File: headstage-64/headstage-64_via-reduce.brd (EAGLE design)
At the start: 19.3 x 19 mm, 169 parts, among them J3 GND_LINK_0201, U1 TS4231, U11 10M08DC, U12 LT3463, U13 DAC5311, U14 TS4231, U15 INA826, U16 TLV70733, U17 TLV70712, U18 TLV70733, U19 DS90UB913A_WQFN, U2 MPU9250_QFN_NO-PAD, U22 TPS62621, U25 TPL0501_UQFN, U3 CAT4016_QFN, U4 OPA170, U5 TS4231, U6 TS4231, U7 RHD2064_BGA, U8 ADG1401, U9 TLV70725

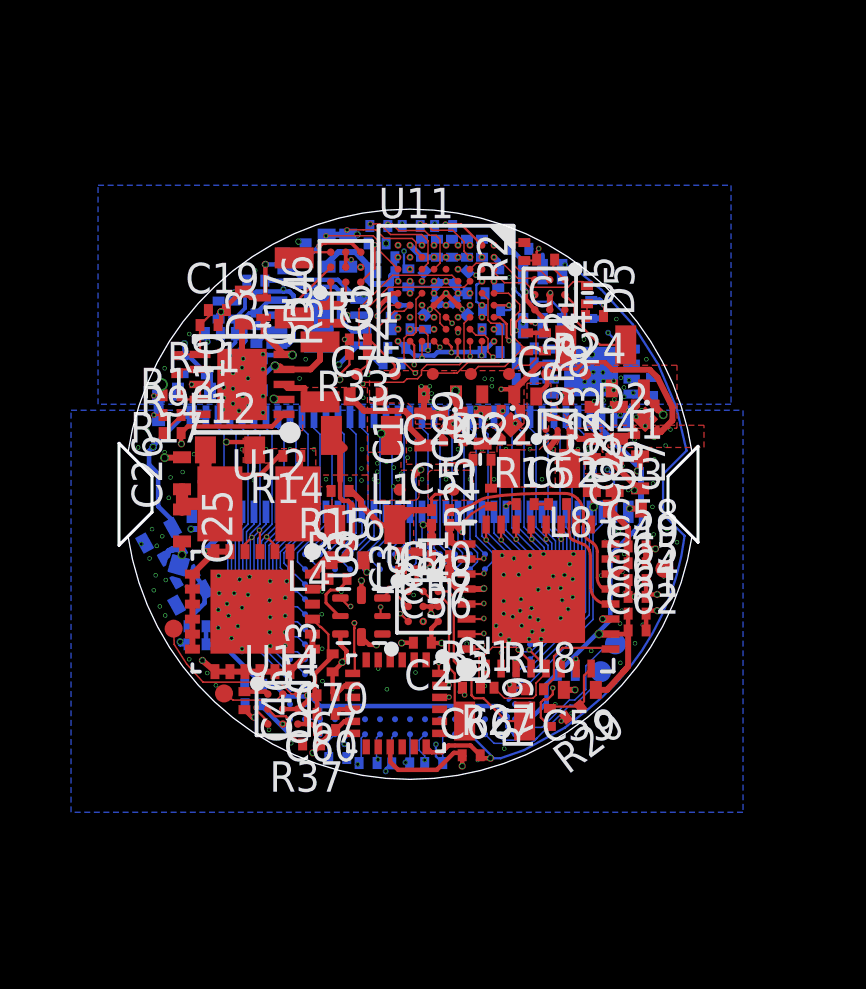
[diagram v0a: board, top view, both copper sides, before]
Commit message: Headstage-64 updates following testing
- Added 50 MHz crystal oscillator to drive FPGA PLL
- LED driver now gets serial data via common MOSI line instead of
dedicated SDO. Clock line is still separate since it acts like the LED
driver's clock and CS together.
- LED driver's blank pin is now tied to CRC_ERROR/C5 on FPGA
- Removed one status LED and instead routed serializer GPIO0 to FPGA
- Increased size of programming pads
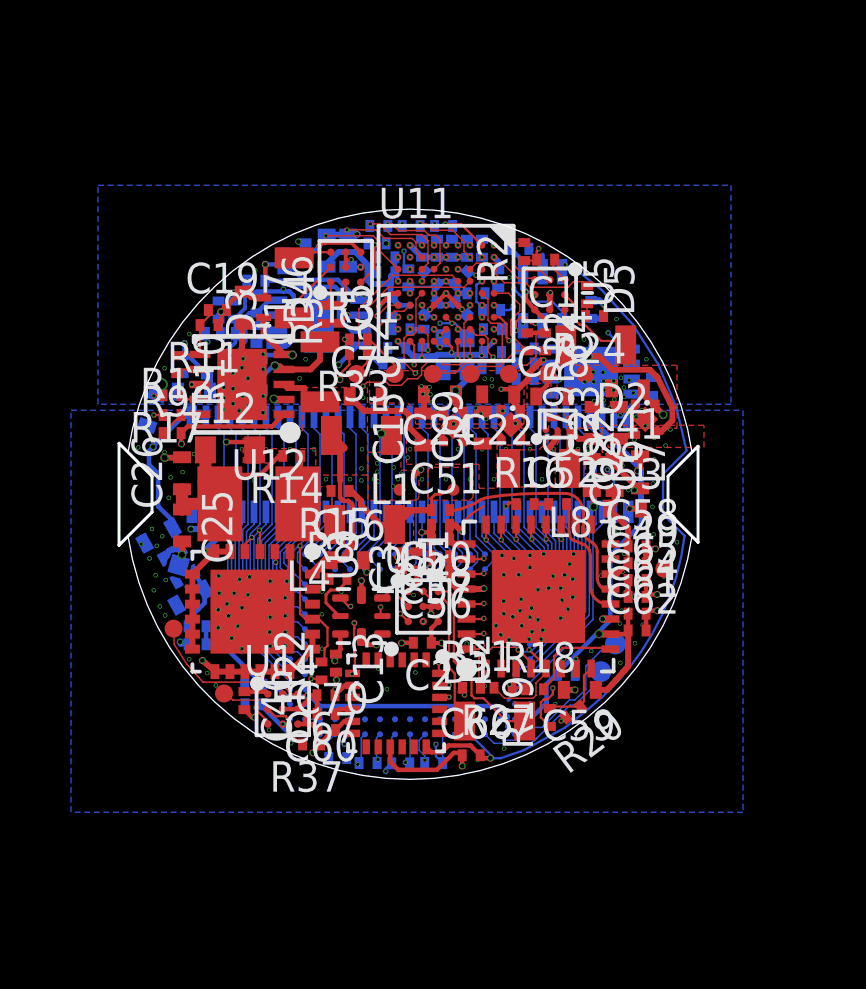
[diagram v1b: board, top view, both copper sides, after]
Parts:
- removed D6: XZVGR155W, jonnew:LED-0201T
- removed J3: GND_LINK_0201, jonnew:0201_LINK
- removed R25: 2k, jonnew:0201T
- added C54: 10nF, jonnew:0201T
- added L13: BLM15PX601SN1D, jonnew:0402T
- added R22: 10k, jonnew:0201T
- added U26: ASCO-50.000MHZ-EK-T3, jonnew:ASCO
- TP1, TP12, TP2, TP3, TP4, TP5, TP6: device jonnew:B0.4MM -> jonnew:TP06R
- moved C13 0.11 mm to (-2.47, -5.63), turned to 270 degrees
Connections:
- net STATUS_B renamed STATUS
- removed net GPO0: TP7.TP, U19.15
- removed net LED_SIN: U11.F1, U3.2
- removed net N$39: D6.2, R25.2
- removed net SDO: U11.E3, U13.3, U2.9
- removed net STATUS_A: D6.1, U11.C2
- new net GPIO0: TP7.TP, U11.C2, U19.15
- new net LED_BLANK: R22.2, U11.C5, U3.21
- new net MOSI: U11.E3, U13.3, U2.9, U3.2
- new net N$37: U11.F1, U26.3
- net +3V3: now also C54.1, R22.1, U26.1, U26.4; no longer R25.1
- net AGND: now also L13.2; no longer J3.1
- net GND: now also C54.2, L13.1, U26.2; no longer J3.2, U3.21
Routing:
- net MOSI: track 0.00 -> 28.1 mm, vias 0 -> 6
- net LED_BLANK: track 0.00 -> 24.4 mm, vias 0 -> 2
- net SDO: track 22.0 -> 0.00 mm, vias 4 -> 0
- net GPIO0: track 0.00 -> 21.5 mm, vias 0 -> 3
- net LED_SIN: track 19.5 -> 0.00 mm, vias 2 -> 0
- net STATUS_A: track 8.32 -> 0.00 mm, vias 2 -> 0
- net GND: track 41.7 -> 38.3 mm, vias 184 -> 186
- net N$37: track 0.00 -> 3.38 mm, vias 0 -> 2
- net GPO0: track 1.99 -> 0.00 mm, vias 2 -> 0
- net +3V3: track 30.4 -> 31.5 mm, vias 21 -> 23
- net N$39: track 0.95 -> 0.00 mm
- net +2V5: track 23.1 -> 23.4 mm, vias 6 -> 8
- added copper zone on layer 4, net +2V5
- added copper zone on layer 1, net GPIO0
- added copper zone on layer 2, net GPIO0
- added copper zone on layer 3, net GPIO0
- added copper zone on layer 1, net LED_BLANK
- added copper zone on layer 3, net LED_BLANK
- added copper zone on layer 1, net MOSI
- added copper zone on layer 16, net MOSI
- added copper zone on layer 2, net MOSI
- added copper zone on layer 3, net MOSI
- added copper zone on layer 16, net N$37
- added copper zone on layer 2, net N$37
- removed copper zone on layer 1, net GPO0
- removed copper zone on layer 3, net GPO0
- removed copper zone on layer 1, net LED_SIN
- removed copper zone on layer 3, net LED_SIN
- removed copper zone on layer 1, net SDO
- removed copper zone on layer 16, net SDO
- removed copper zone on layer 2, net SDO
- removed copper zone on layer 3, net SDO
- removed copper zone on layer 1, net STATUS_A
- removed copper zone on layer 3, net STATUS_A

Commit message: Updates due to production questions from speedy
- Space added between some components
- 3.3V stub removed from headstage-64
- Intan AUXOUTs routed to test points on both boards
- Crystal's re-routed to drive FPGA clock pins that interface with an
avaialble PLL. Previous routing went to clock pins that had no PLL on
both designs.
- Some pins swapping to simplfy routing on both boards.
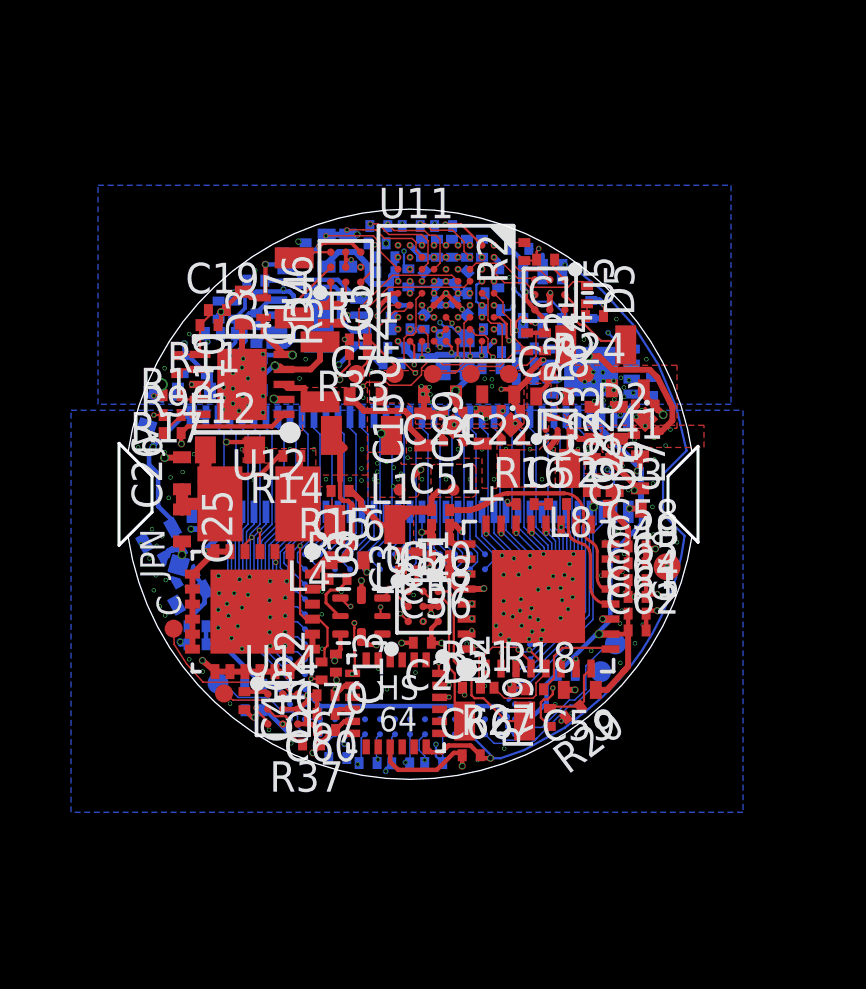
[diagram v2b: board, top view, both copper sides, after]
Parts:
- added TP13: VCC, jonnew:TP07R
- TP7: device jonnew:TP06R -> jonnew:TP09R
- moved C30 0.20 mm to (-5.20, -7.20)
- moved TP7 0.11 mm to (8.57, -2.42)
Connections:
- new net N$39: TP13.TP, U7.N16
- net DAC_CS: now also U11.C2; no longer U11.C4
- net DATA4: now also U11.B6; no longer U11.G3
- net ENV2: now also U11.F1; no longer U11.D8
- net ENV4: now also U11.G3; no longer U11.B6
- net GPIO0: now also U11.A5; no longer U11.C2
- net N$37: now also U11.D8; no longer U11.F1
- net STIM_NULL: now also U11.C4; no longer U11.A5
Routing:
- net N$39: track 0.00 -> 4.06 mm
- net ENV4: track 23.2 -> 20.2 mm, vias 2 -> 3
- net ENV2: track 4.43 -> 1.50 mm
- net GPIO0: track 21.5 -> 18.8 mm
- net DATA4: track 20.2 -> 22.1 mm, vias 3 -> 2
- net +3V3: track 31.5 -> 30.2 mm
- net DAC_CS: track 4.53 -> 3.73 mm
- net DIN0: track 9.56 -> 8.76 mm
- net STIM_NULL: track 8.02 -> 7.27 mm
- net DIN7: track 11.1 -> 10.4 mm
- net DIN6: track 10.0 -> 9.43 mm
- net DIN10: track 13.6 -> 13.1 mm
- net DIN8: track 11.7 -> 11.1 mm
- net TDI: track 5.15 -> 4.62 mm
- net GND: vias 186 -> 187
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- added copper zone on layer 1, net ENV4
- added copper zone on layer 3, net ENV4
- removed copper zone on layer 3, net DATA4
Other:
- board text added: "+"
- board text added: "-"
- board text added: "0"
- board text added: "C"
- board text added: "COHLv1.2"
- board text added: "G"
- board text added: "HS 64"
- board text added: "HS-64 Rev 1.1"
- board text added: "JPN"
- board text added: "JPN&JV MIT,'18"
- board text added: "JV"
- board text removed: "HS-64 Rev 1.0"
- board text removed: "JPN,JV COHL v1.2"

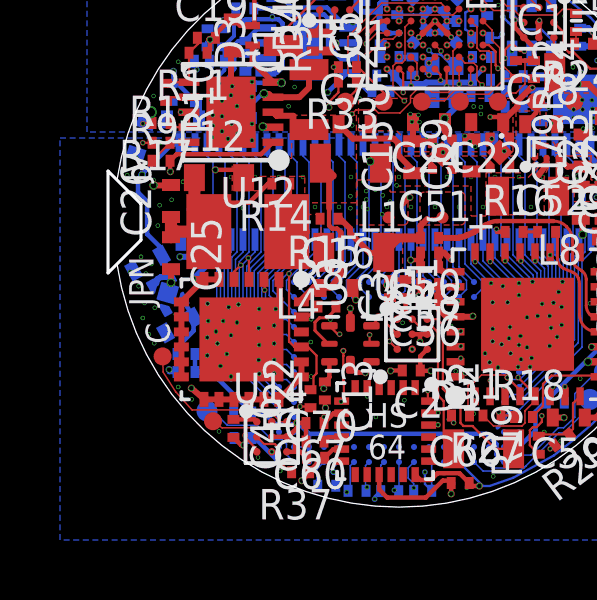
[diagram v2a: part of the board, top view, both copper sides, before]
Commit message: Added AGND testpoints to bottom of headstage-64 and headstage-256
- So that people can actually use the other IO test points...
- These are ready for production
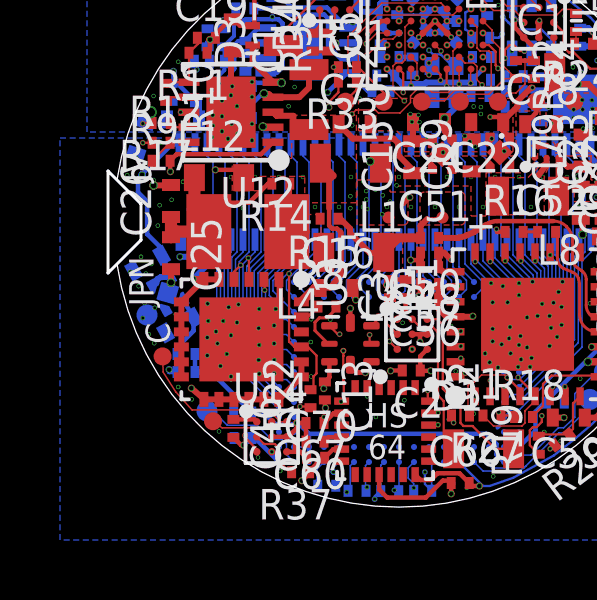
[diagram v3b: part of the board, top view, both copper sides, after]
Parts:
- added TP14: VCC, jonnew:TP07R
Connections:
- net AGND: now also TP14.TP
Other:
- board text added: "IN2"
- board text added: "IN3"
- board text added: "O"
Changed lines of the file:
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@@
 <setting verticaltext="up"/>
 </settings>
-<grid distance="0.05" unitdist="mm" unit="mm" style="lines" multiple="1" display="yes" altdistance="0.1" altunitdist="mm" altunit="mm"/>
+<grid distance="0.1" unitdist="mm" unit="mm" style="lines" multiple="1" display="yes" altdistance="0.1" altunitdist="mm" altunit="mm"/>
 <layers>
 <layer number="1" name="Top" color="4" fill="1" visible="yes" active="yes"/>
@@
 <layer number="19" name="Unrouted" color="14" fill="1" visible="yes" active="yes"/>
 <layer number="20" name="Dimension" color="15" fill="1" visible="yes" active="yes"/>
-<layer number="21" name="tPlace" color="7" fill="1" visible="yes" active="yes"/>
+<layer number="21" name="tPlace" color="7" fill="1" visible="no" active="yes"/>
 <layer number="22" name="bPlace" color="7" fill="1" visible="yes" active="yes"/>
-<layer number="23" name="tOrigins" color="15" fill="1" visible="yes" active="yes"/>
+<layer number="23" name="tOrigins" color="15" fill="1" visible="no" active="yes"/>
 <layer number="24" name="bOrigins" color="15" fill="1" visible="yes" active="yes"/>
 <layer number="25" name="tNames" color="7" fill="1" visible="no" active="yes"/>
@@
 <layer number="27" name="tValues" color="7" fill="1" visible="no" active="yes"/>
 <layer number="28" name="bValues" color="7" fill="1" visible="no" active="yes"/>
-<layer number="29" name="tStop" color="7" fill="3" visible="yes" active="yes"/>
+<layer number="29" name="tStop" color="7" fill="3" visible="no" active="yes"/>
 <layer number="30" name="bStop" color="7" fill="6" visible="yes" active="yes"/>
 <layer number="31" name="tCream" color="7" fill="4" visible="no" active="yes"/>
@@
 <layer number="37" name="tTest" color="7" fill="1" visible="no" active="yes"/>
 <layer number="38" name="bTest" color="7" fill="1" visible="no" active="yes"/>
-<layer number="39" name="tKeepout" color="4" fill="11" visible="yes" active="yes"/>
-<layer number="40" name="bKeepout" color="1" fill="11" visible="yes" active="yes"/>
+<layer number="39" name="tKeepout" color="4" fill="11" visible="no" active="yes"/>
+<layer number="40" name="bKeepout" color="1" fill="11" visible="no" active="yes"/>
 <layer number="41" name="tRestrict" color="4" fill="10" visible="no" active="yes"/>
 <layer number="42" name="bRestrict" color="1" fill="10" visible="no" active="yes"/>
@@
 <layer number="49" name="Reference" color="7" fill="1" visible="no" active="yes"/>
 <layer number="50" name="dxf" color="7" fill="1" visible="no" active="no"/>
-<layer number="51" name="tDocu" color="7" fill="1" visible="yes" active="yes"/>
-<layer number="52" name="bDocu" color="7" fill="1" visible="yes" active="yes"/>
+<layer number="51" name="tDocu" color="7" fill="1" visible="no" active="yes"/>
+<layer number="52" name="bDocu" color="7" fill="1" visible="no" active="yes"/>
 <layer number="53" name="tGND_GNDA" color="7" fill="9" visible="no" active="no"/>
 <layer number="54" name="bGND_GNDA" color="1" fill="9" visible="no" active="no"/>
@@
 <text x="-8.59001875" y="-1.9800125" size="0.8128" layer="21" font="vector" ratio="19" distance="30" rot="R90" align="center">JPN</text>
 <text x="-8.79001875" y="1.8199875" size="0.8128" layer="21" font="vector" ratio="19" distance="30" rot="R90" align="center">JV</text>
+<text x="-8.758478125" y="-2.41385625" size="0.8128" layer="22" font="vector" ratio="19" distance="30" rot="MR334.2" align="center">G</text>
+<text x="5.48" y="-7.03" size="0.8128" layer="22" font="vector" ratio="19" distance="30" rot="MR141.8" align="center">IN2</text>
+<text x="7.86" y="-4.15" size="0.8128" layer="22" font="vector" ratio="19" distance="30" rot="MR298.4" align="center">IN3</text>
+<text x="-7.02" y="-5.76" size="0.8128" layer="22" font="vector" ratio="19" distance="30" rot="MR315.1" align="center">O</text>
 </plain>
 <attributes>
@@
 <attribute name="TP_SIGNAL_NAME" value="" x="-6.4" y="-6.3" size="1.778" layer="28" rot="MR0" display="off"/>
 </element>
+<element name="TP14" library="jonnew" package="TP07R" value="VCC" x="-8.4" y="-3.1" rot="MR0">
+<attribute name="TP_SIGNAL_NAME" value="" x="-8.4" y="-3.1" size="1.778" layer="28" rot="MR0" display="off"/>
+</element>
 </elements>
 <signals>
@@
 <via x="4" y="-8" extent="5-16" drill="0.1"/>
 <contactref element="L13" pad="2"/>
+<contactref element="TP14" pad="TP"/>
 </signal>
 <signal name="RHD_CS_-">
